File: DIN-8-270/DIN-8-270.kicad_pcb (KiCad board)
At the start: 2 copper layers, 60 x 59.5 mm, 3 parts, among them J1 Socket, J2 Pins, J3 Breakout

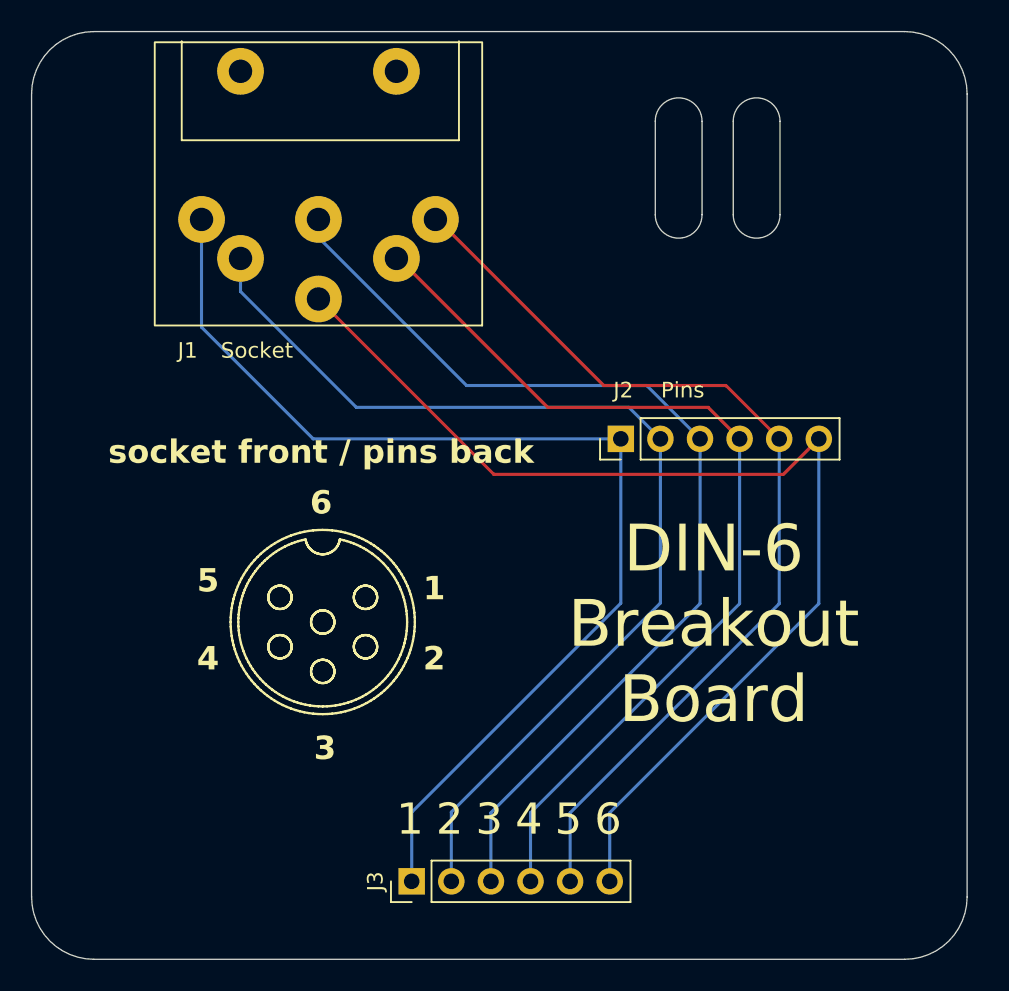
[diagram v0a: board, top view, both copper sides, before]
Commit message: Improve layouts, add DIN-8 270° board.
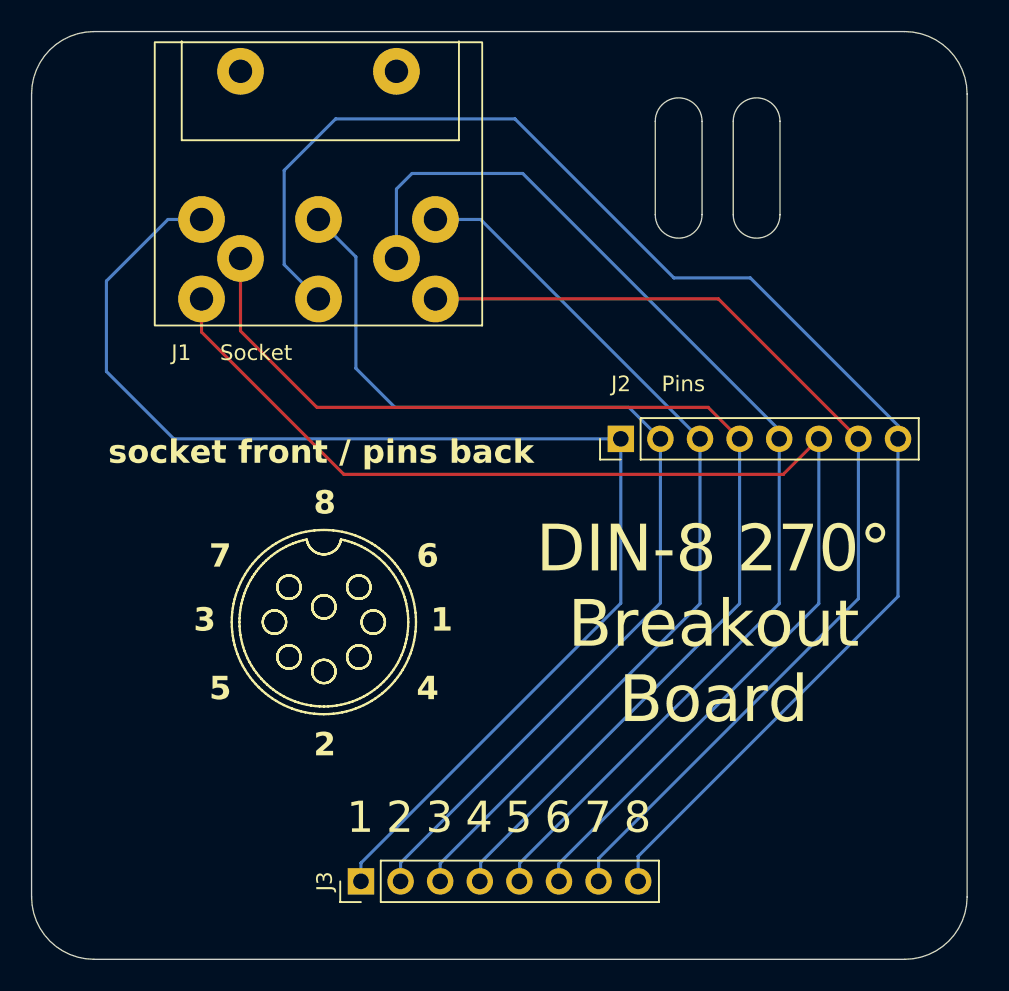
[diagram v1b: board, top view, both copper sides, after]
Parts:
- J1: footprint T-Pau:DIN-6 -> T-Pau:DIN-8-270
- J2, J3: footprint Connector_PinHeader_2.54mm:PinHeader_1x06_P2.54mm_Vertical -> Connector_PinHeader_2.54mm:PinHeader_1x08_P2.54mm_Vertical
- moved J3 3.25 mm to (91.1, 118.5)
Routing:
- net Net-(J2-Pin_8): track 0.00 -> 94.2 mm
- net Net-(J2-Pin_7): track 0.00 -> 66.1 mm
- net Net-(J2-Pin_4): track 60.7 -> 74.7 mm
- net Net-(J2-Pin_1): track 70.7 -> 83.6 mm
- net Net-(J2-Pin_6): track 71.6 -> 81.7 mm
- net Net-(J2-Pin_5): track 61.8 -> 71.5 mm
- net Net-(J2-Pin_3): track 64.9 -> 58.1 mm
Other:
- board text added: "7"
- board text added: "8"
- board text added: "DIN-8 270° Breakout Board"
- board text added: "DIN-8 270° Breakout Board ©2025 Dieter Baron github.com/T-Pau/Connector-Breakout-Boards"
- board text removed: "DIN-6 Breakout Board"
- board text removed: "DIN-6 Breakout Board ©2025 Dieter Baron github.com/T-Pau/Connector-Breakout-Boards"

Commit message: Begin SCART breakout board.
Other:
- board text added: "DIN-8 270° Breakout Board Revision 1 ©2025 Dieter Baron github.com/T-Pau/Connector-Breakout-Boards"
- board text removed: "DIN-8 270° Breakout Board ©2025 Dieter Baron github.com/T-Pau/Connector-Breakout-Boards"
